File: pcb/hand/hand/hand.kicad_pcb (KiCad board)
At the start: 2 copper layers, 172.5 x 135.2 mm, 44 parts, among them J1 Conn_01x15, J2 Conn_01x15

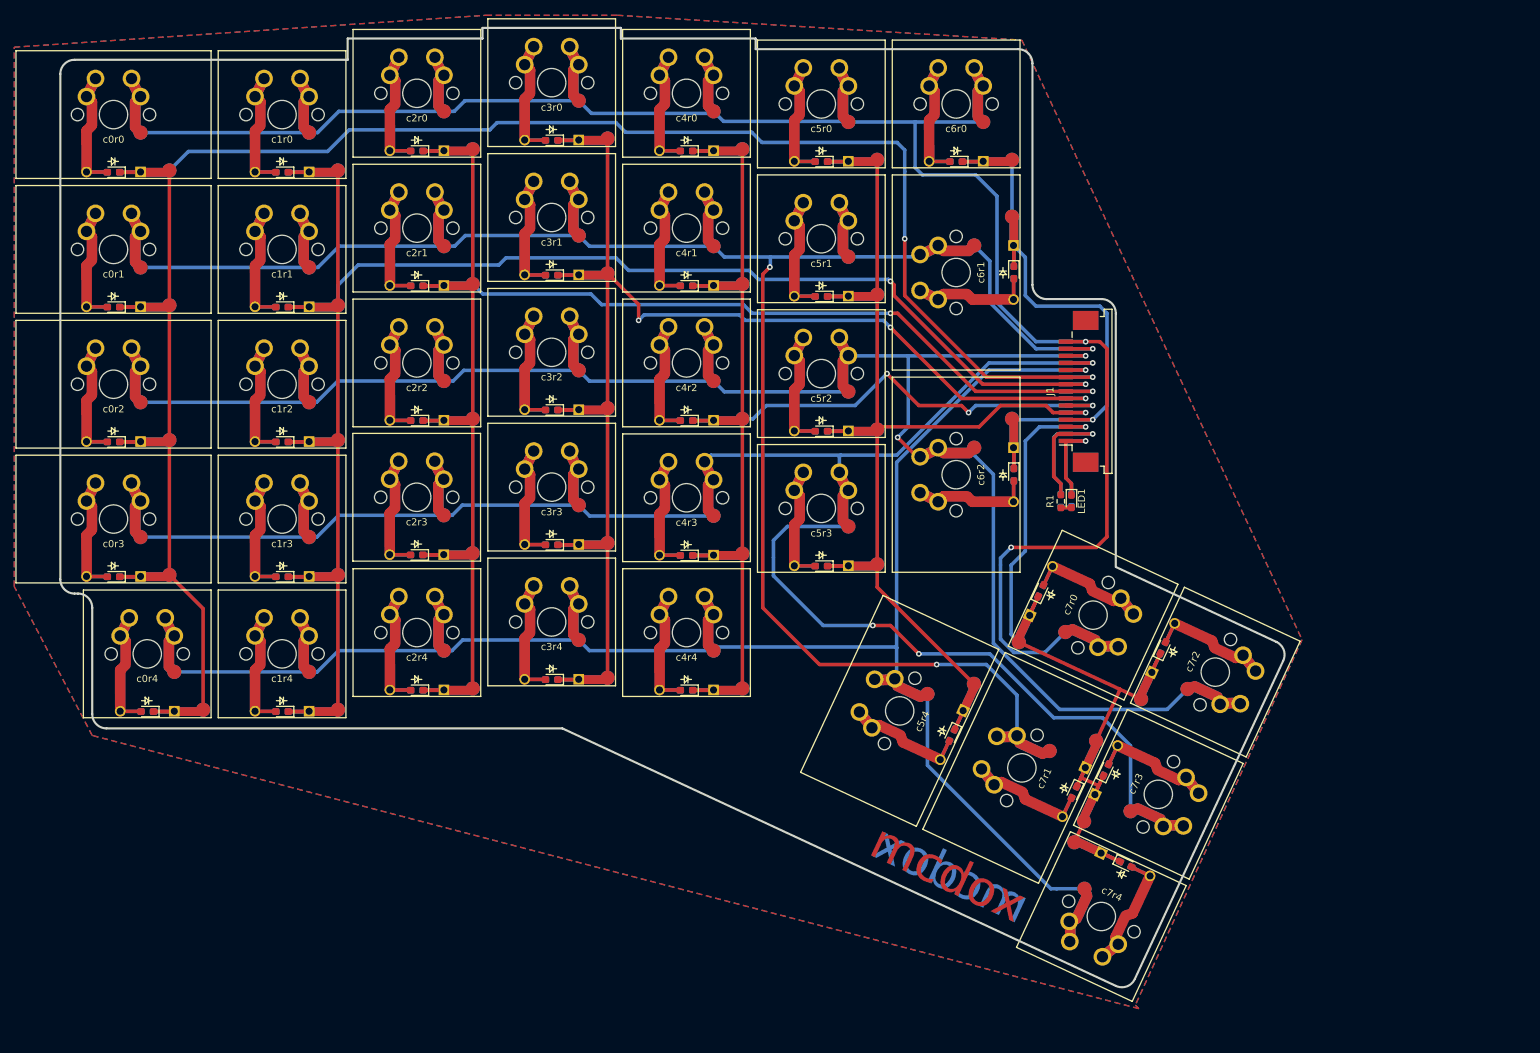
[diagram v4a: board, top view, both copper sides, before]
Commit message: pcb/hand Mounting holes for standoff tenting.
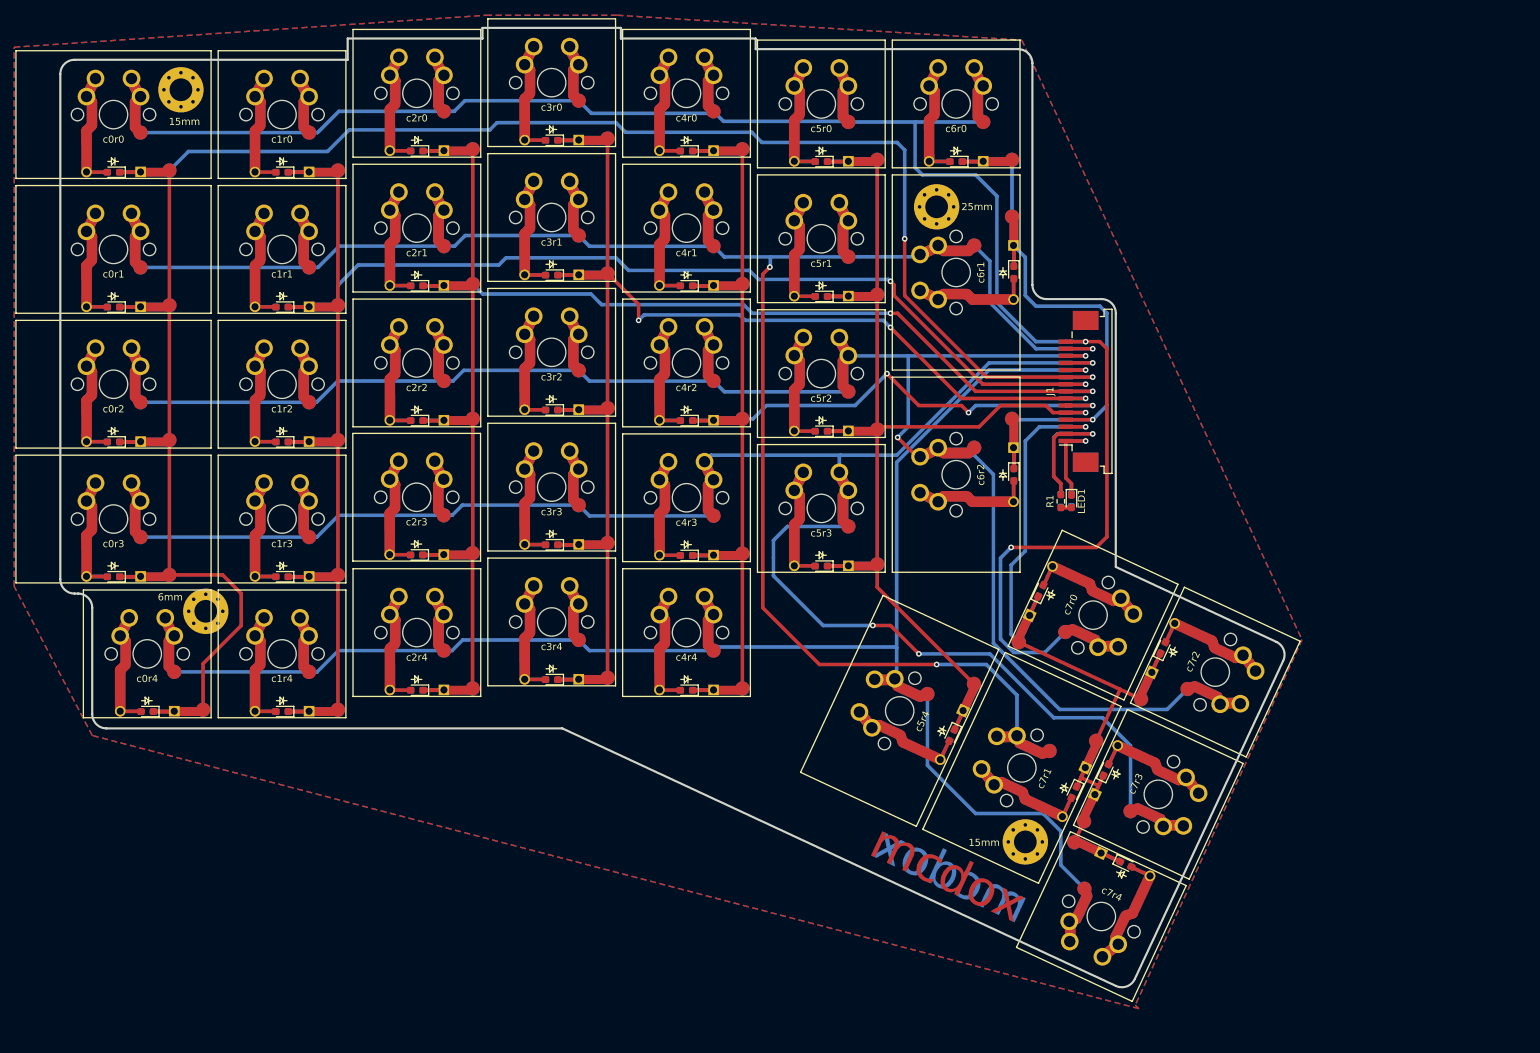
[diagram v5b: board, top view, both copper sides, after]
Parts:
- added 15mm: MountingHole_3.2mm_M3_Pad_Via, MountingHole:MountingHole_3.2mm_M3_Pad_Via, F.Cu at (172.5, 141.5)
- added 15mm: MountingHole_3.2mm_M3_Pad_Via, MountingHole:MountingHole_3.2mm_M3_Pad_Via, F.Cu at (53.5, 35.5)
- added 25mm: MountingHole_3.2mm_M3_Pad_Via, MountingHole:MountingHole_3.2mm_M3_Pad_Via, F.Cu at (160.0, 52.0)
- added 6mm: MountingHole_3.2mm_M3_Pad_Via, MountingHole:MountingHole_3.2mm_M3_Pad_Via, F.Cu at (57.0, 109.0)
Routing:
- net col0: track 312.6 -> 321.4 mm
- net row4: track 242.2 -> 245.0 mm
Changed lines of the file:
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@@
   (general
     (thickness 1.6)
-    (drawings 30)
-    (tracks 715)
+    (drawings 33)
+    (tracks 720)
     (zones 0)
-    (modules 44)
+    (modules 48)
     (nets 18)
   )
@@
     (add_net row4)
   )
+  (module MountingHole:MountingHole_3.2mm_M3_Pad_Via (layer F.Cu)
+    (at 172.5 141.5)
+    (descr "Mounting Hole 3.2mm, M3")
+    (tags "mounting hole 3.2mm m3")
+    (attr virtual)
+    (fp_text reference 15mm (at -5.8 0.1) (layer F.SilkS)
+      (effects (font (size 1 1) (thickness 0.15)))
+    )
+    (fp_text value MountingHole_3.2mm_M3_Pad_Via (at 0 4.2) (layer F.Fab)
+      (effects (font (size 1 1) (thickness 0.15)))
+    )
+    (fp_text user %R (at 0.3 0) (layer F.Fab)
+      (effects (font (size 1 1) (thickness 0.15)))
+    )
+    (fp_circle (center 0 0) (end 3.2 0) (layer Cmts.User) (width 0.15))
+    (fp_circle (center 0 0) (end 3.45 0) (layer F.CrtYd) (width 0.05))
+    (pad 1 thru_hole circle (at 1.697056 -1.697056) (size 0.8 0.8) (drill 0.5) (layers *.Cu *.Mask))
+    (pad 1 thru_hole circle (at 0 -2.4) (size 0.8 0.8) (drill 0.5) (layers *.Cu *.Mask))
+    (pad 1 thru_hole circle (at -1.697056 -1.697056) (size 0.8 0.8) (drill 0.5) (layers *.Cu *.Mask))
+    (pad 1 thru_hole circle (at -2.4 0) (size 0.8 0.8) (drill 0.5) (layers *.Cu *.Mask))
+    (pad 1 thru_hole circle (at -1.697056 1.697056) (size 0.8 0.8) (drill 0.5) (layers *.Cu *.Mask))
+    (pad 1 thru_hole circle (at 0 2.4) (size 0.8 0.8) (drill 0.5) (layers *.Cu *.Mask))
+    (pad 1 thru_hole circle (at 1.697056 1.697056) (size 0.8 0.8) (drill 0.5) (layers *.Cu *.Mask))
+    (pad 1 thru_hole circle (at 2.4 0) (size 0.8 0.8) (drill 0.5) (layers *.Cu *.Mask))
+    (pad 1 thru_hole circle (at 0 0) (size 6.4 6.4) (drill 3.2) (layers *.Cu *.Mask))
+  )
+  (module MountingHole:MountingHole_3.2mm_M3_Pad_Via (layer F.Cu)
+    (at 160 52)
+    (descr "Mounting Hole 3.2mm, M3")
+    (tags "mounting hole 3.2mm m3")
+    (attr virtual)
+    (fp_text reference 25mm (at 5.7 0) (layer F.SilkS)
+      (effects (font (size 1 1) (thickness 0.15)))
+    )
+    (fp_text value MountingHole_3.2mm_M3_Pad_Via (at 0 4.2) (layer F.Fab)
+      (effects (font (size 1 1) (thickness 0.15)))
+    )
+    (fp_text user %R (at 0.3 0) (layer F.Fab)
+      (effects (font (size 1 1) (thickness 0.15)))
+    )
+    (fp_circle (center 0 0) (end 3.2 0) (layer Cmts.User) (width 0.15))
+    (fp_circle (center 0 0) (end 3.45 0) (layer F.CrtYd) (width 0.05))
+    (pad 1 thru_hole circle (at 1.697056 -1.697056) (size 0.8 0.8) (drill 0.5) (layers *.Cu *.Mask))
+    (pad 1 thru_hole circle (at 0 -2.4) (size 0.8 0.8) (drill 0.5) (layers *.Cu *.Mask))
+    (pad 1 thru_hole circle (at -1.697056 -1.697056) (size 0.8 0.8) (drill 0.5) (layers *.Cu *.Mask))
+    (pad 1 thru_hole circle (at -2.4 0) (size 0.8 0.8) (drill 0.5) (layers *.Cu *.Mask))
+    (pad 1 thru_hole circle (at -1.697056 1.697056) (size 0.8 0.8) (drill 0.5) (layers *.Cu *.Mask))
+    (pad 1 thru_hole circle (at 0 2.4) (size 0.8 0.8) (drill 0.5) (layers *.Cu *.Mask))
+    (pad 1 thru_hole circle (at 1.697056 1.697056) (size 0.8 0.8) (drill 0.5) (layers *.Cu *.Mask))
+    (pad 1 thru_hole circle (at 2.4 0) (size 0.8 0.8) (drill 0.5) (layers *.Cu *.Mask))
+    (pad 1 thru_hole circle (at 0 0) (size 6.4 6.4) (drill 3.2) (layers *.Cu *.Mask))
+  )
+  (module MountingHole:MountingHole_3.2mm_M3_Pad_Via (layer F.Cu)
+    (at 57 109)
+    (descr "Mounting Hole 3.2mm, M3")
+    (tags "mounting hole 3.2mm m3")
+    (attr virtual)
+    (fp_text reference 6mm (at -5 -2) (layer F.SilkS)
+      (effects (font (size 1 1) (thickness 0.15)))
+    )
+    (fp_text value MountingHole_3.2mm_M3_Pad_Via (at 0 4.2) (layer F.Fab)
+      (effects (font (size 1 1) (thickness 0.15)))
+    )
+    (fp_text user %R (at 0.3 0) (layer F.Fab)
+      (effects (font (size 1 1) (thickness 0.15)))
+    )
+    (fp_circle (center 0 0) (end 3.2 0) (layer Cmts.User) (width 0.15))
+    (fp_circle (center 0 0) (end 3.45 0) (layer F.CrtYd) (width 0.05))
+    (pad 1 thru_hole circle (at 1.697056 -1.697056) (size 0.8 0.8) (drill 0.5) (layers *.Cu *.Mask))
+    (pad 1 thru_hole circle (at 0 -2.4) (size 0.8 0.8) (drill 0.5) (layers *.Cu *.Mask))
+    (pad 1 thru_hole circle (at -1.697056 -1.697056) (size 0.8 0.8) (drill 0.5) (layers *.Cu *.Mask))
+    (pad 1 thru_hole circle (at -2.4 0) (size 0.8 0.8) (drill 0.5) (layers *.Cu *.Mask))
+    (pad 1 thru_hole circle (at -1.697056 1.697056) (size 0.8 0.8) (drill 0.5) (layers *.Cu *.Mask))
+    (pad 1 thru_hole circle (at 0 2.4) (size 0.8 0.8) (drill 0.5) (layers *.Cu *.Mask))
+    (pad 1 thru_hole circle (at 1.697056 1.697056) (size 0.8 0.8) (drill 0.5) (layers *.Cu *.Mask))
+    (pad 1 thru_hole circle (at 2.4 0) (size 0.8 0.8) (drill 0.5) (layers *.Cu *.Mask))
+    (pad 1 thru_hole circle (at 0 0) (size 6.4 6.4) (drill 3.2) (layers *.Cu *.Mask))
+  )
+  (module MountingHole:MountingHole_3.2mm_M3_Pad_Via (layer F.Cu)
+    (at 53.5 35.5)
+    (descr "Mounting Hole 3.2mm, M3")
+    (tags "mounting hole 3.2mm m3")
+    (attr virtual)
+    (fp_text reference 15mm (at 0.5 4.5) (layer F.SilkS)
+      (effects (font (size 1 1) (thickness 0.15)))
+    )
+    (fp_text value MountingHole_3.2mm_M3_Pad_Via (at 0 4.2) (layer F.Fab)
+      (effects (font (size 1 1) (thickness 0.15)))
+    )
+    (fp_text user %R (at 0.3 0) (layer F.Fab)
+      (effects (font (size 1 1) (thickness 0.15)))
+    )
+    (fp_circle (center 0 0) (end 3.2 0) (layer Cmts.User) (width 0.15))
+    (fp_circle (center 0 0) (end 3.45 0) (layer F.CrtYd) (width 0.05))
+    (pad 1 thru_hole circle (at 1.697056 -1.697056) (size 0.8 0.8) (drill 0.5) (layers *.Cu *.Mask))
+    (pad 1 thru_hole circle (at 0 -2.4) (size 0.8 0.8) (drill 0.5) (layers *.Cu *.Mask))
+    (pad 1 thru_hole circle (at -1.697056 -1.697056) (size 0.8 0.8) (drill 0.5) (layers *.Cu *.Mask))
+    (pad 1 thru_hole circle (at -2.4 0) (size 0.8 0.8) (drill 0.5) (layers *.Cu *.Mask))
+    (pad 1 thru_hole circle (at -1.697056 1.697056) (size 0.8 0.8) (drill 0.5) (layers *.Cu *.Mask))
+    (pad 1 thru_hole circle (at 0 2.4) (size 0.8 0.8) (drill 0.5) (layers *.Cu *.Mask))
+    (pad 1 thru_hole circle (at 1.697056 1.697056) (size 0.8 0.8) (drill 0.5) (layers *.Cu *.Mask))
+    (pad 1 thru_hole circle (at 2.4 0) (size 0.8 0.8) (drill 0.5) (layers *.Cu *.Mask))
+    (pad 1 thru_hole circle (at 0 0) (size 6.4 6.4) (drill 3.2) (layers *.Cu *.Mask))
+  )
   (module Resistor_SMD:R_0603_1608Metric_Pad0.98x0.95mm_HandSolder (layer B.Cu)
     (at 177.5 93.4125 270)
@@
     )
   )
+  (gr_line (start 121.1 95.7) (end 160 52) (layer Dwgs.User) (width 0.15))
+  (gr_line (start 57 109) (end 91.9 69.8) (layer Dwgs.User) (width 0.15))
+  (gr_line (start 53.5 35.5) (end 172.5 141.5) (layer Dwgs.User) (width 0.15))
   (gr_text mcdox (at 162.071666 146.126735 -25) (layer B.Cu)
     (effects (font (size 5 5) (thickness 0.3)) (justify mirror))
@@
   (segment (start 51.874 65.874) (end 51.874 84.874) (width 0.5) (layer F.Cu) (net 1))
   (segment (start 51.874 84.874) (end 51.874 103.874) (width 0.5) (layer F.Cu) (net 1))
-  (segment (start 56.624 108.624) (end 56.624 122.874) (width 0.5) (layer F.Cu) (net 1))
-  (segment (start 51.874 103.874) (end 56.624 108.624) (width 0.5) (layer F.Cu) (net 1))
   (segment (start 56.37 123.128) (end 56.624 122.874) (width 0.5) (layer B.Cu) (net 1))
   (segment (start 49.625 123.128) (end 56.37 123.128) (width 0.5) (layer B.Cu) (net 1))
@@
   (segment (start 167 76) (end 155.5 64.5) (width 0.5) (layer F.Cu) (net 1))
   (segment (start 178.2 76) (end 167 76) (width 0.5) (layer F.Cu) (net 1))
+  (segment (start 51.874 103.874) (end 59.374 103.874) (width 0.5) (layer F.Cu) (net 1))
+  (segment (start 59.374 103.874) (end 62 106.5) (width 0.5) (layer F.Cu) (net 1))
+  (segment (start 62 106.5) (end 62 111) (width 0.5) (layer F.Cu) (net 1))
+  (segment (start 56.624 116.376) (end 56.624 122.874) (width 0.5) (layer F.Cu) (net 1))
+  (segment (start 62 111) (end 56.624 116.376) (width 0.5) (layer F.Cu) (net 1))
   (segment (start 128.274999 38.825001) (end 128.56 38.54) (width 0.5) (layer B.Cu) (net 2))
   (segment (start 111.345001 38.825001) (end 128.274999 38.825001) (width 0.5) (layer B.Cu) (net 2))
@@
   (segment (start 178.515417 154.866745) (end 178.761132 155.54184) (width 0.5) (layer F.Cu) (net 6))
   (segment (start 178.837453 154.176139) (end 178.515417 154.866745) (width 0.5) (layer F.Cu) (net 6))
-  (segment (start 176.924821 148.099049) (end 180.830472 148.099049) (width 0.5) (layer B.Cu) (net 6))
-  (segment (start 176.099049 148.099049) (end 176.924821 148.099049) (width 0.5) (layer B.Cu) (net 6))
-  (segment (start 158.704866 121.27819) (end 158.704866 130.704866) (width 0.5) (layer B.Cu) (net 6))
-  (segment (start 158.704866 130.704866) (end 176.099049 148.099049) (width 0.5) (layer B.Cu) (net 6))
   (via (at 181 75) (size 0.8) (drill 0.4) (layers F.Cu B.Cu) (net 6))
   (segment (start 178.2 75) (end 181 75) (width 0.5) (layer F.Cu) (net 6))
@@
   (segment (start 151.338397 118.664264) (end 151.262076 118.587943) (width 0.5) (layer B.Cu) (net 6))
   (segment (start 152.627777 118.664264) (end 151.338397 118.664264) (width 0.5) (layer B.Cu) (net 6))
+  (segment (start 165.5 137.5) (end 158.704866 130.704866) (width 0.5) (layer B.Cu) (net 6))
+  (segment (start 158.704866 130.704866) (end 158.704866 121.27819) (width 0.5) (layer B.Cu) (net 6))
+  (segment (start 175 137.5) (end 165.5 137.5) (width 0.5) (layer B.Cu) (net 6))
+  (segment (start 177.5 140) (end 175 137.5) (width 0.5) (layer B.Cu) (net 6))
+  (segment (start 180.830472 148.099049) (end 177.5 144.768577) (width 0.5) (layer B.Cu) (net 6))
+  (segment (start 177.5 144.768577) (end 177.5 140) (width 0.5) (layer B.Cu) (net 6))
   (segment (start 75.624 46.874) (end 75.624 65.874) (width 0.5) (layer F.Cu) (net 7))
   (segment (start 75.624 65.874) (end 75.624 84.874) (width 0.5) (layer F.Cu) (net 7))
